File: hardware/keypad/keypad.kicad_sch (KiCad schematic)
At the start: 11 parts, among them J101 Conn_02x05_Odd_Even

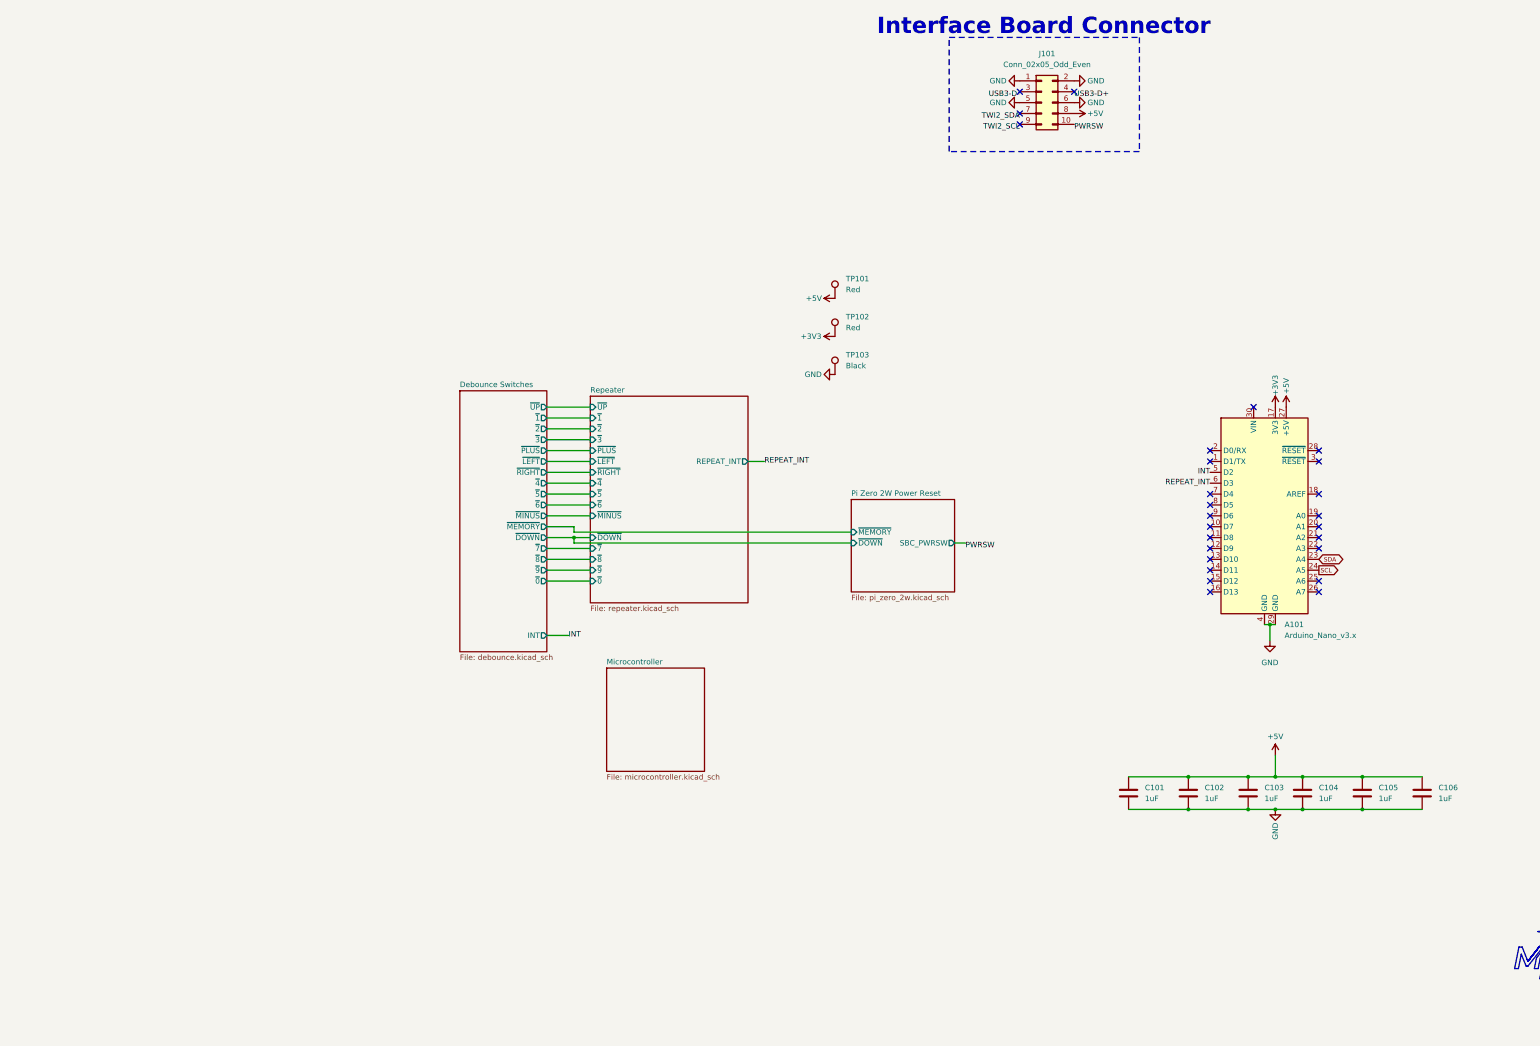
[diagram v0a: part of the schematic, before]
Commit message: Revision X2!
New and improved revision of the keypad! I fixed issues with the repeater and remote SBC power switch circuit (hopefully🤞). I also integrated the Arduino Nano onto the board (ATMEGA328).
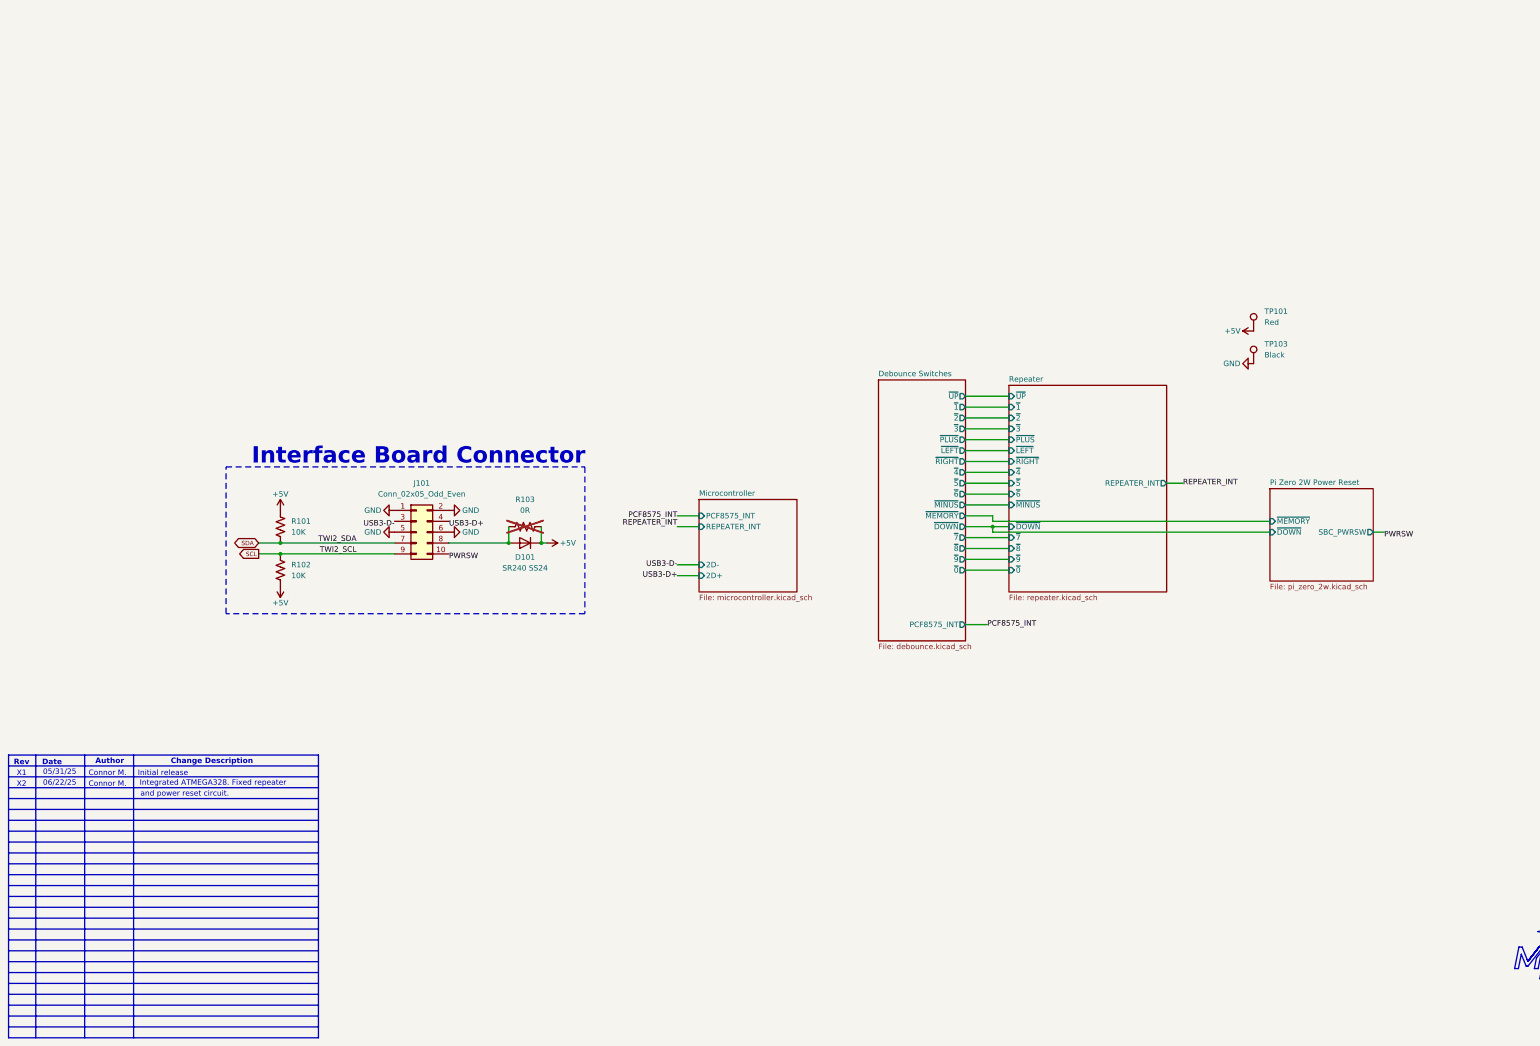
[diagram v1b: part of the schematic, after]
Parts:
- removed A101: Arduino_Nano_v3.x, Module:Arduino_Nano, symbol MCU_Module:Arduino_Nano_v3.x
- removed C101, C102, C103, C104, C105, C106: 1uF, Capacitor_SMD:C_0805_2012Metric, symbol Device:C
- removed TP102: Red, TestPoint:TestPoint_Keystone_5000-5004_Miniature, symbol Connector:TestPoint
- added D101: SR240 SS24, Diode_SMD:D_SMA, symbol Device:D
- added R101, R102: 10K, Resistor_SMD:R_0805_2012Metric, symbol Device:R_US
- added R103: 0R, Resistor_SMD:R_0805_2012Metric, symbol Device:R_US
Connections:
- net TWI2_SCL is gone; now on net SCL: J101.9 (Pin_9)
- net TWI2_SDA is gone; now on net SDA: J101.7 (Pin_7)
- net +5V: now also D101.1 (K), R101.1, R102.2, R103.2; no longer J101.8 (Pin_8)
- net SCL: now also R102.1
- net SDA: now also R101.2
- new net: D101.2 (A), J101.8 (Pin_8), R103.1
- no-connect marks 26 -> 0
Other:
- sheet Debounce Switches ports: added PCF8575_INT; removed INT
- sheet Microcontroller ports: added 2D+, 2D-, PCF8575_INT, REPEATER_INT; removed none
- sheet Repeater ports: added REPEATER_INT; removed REPEAT_INT
- note added: "05/31/25"
- note added: "06/22/25"
- note added: "Author"
- note added: "Change Description"
- note added: "Connor M."
- note added: "Date"
- note added: "Initial release"
- note added: "Integrated ATMEGA328. Fixed repeater"
- note added: "Rev"
- note added: "X1"
- note added: "X2"
- note added: "and power reset circuit."
- moved on the sheet: J101, TP101, TP103
